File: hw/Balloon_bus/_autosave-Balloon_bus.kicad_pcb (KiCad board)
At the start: 16 copper layers, 96 x 89.9 mm, 14 parts, among them J1 3V3, J2 DEPLOY SENSOR, J3 SERVO, J4 SOLENOID, J5 LINEAR ACTUATOR, U1 XA1110, U2 MPU-9250-BREAKOUT-R, U3 BMP180-V2, U4 SN754410

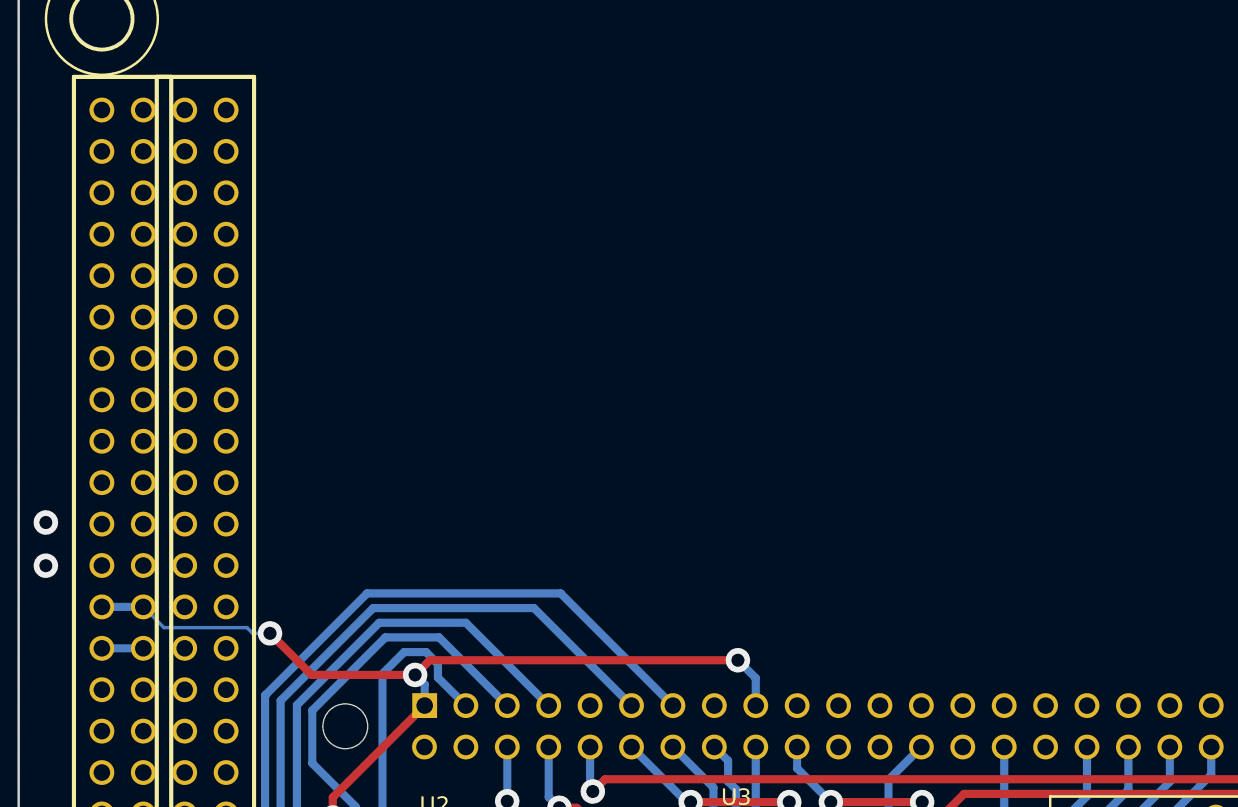
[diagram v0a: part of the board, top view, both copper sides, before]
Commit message: Zero unrouted tracks. Sensors and GPS schematics added to their respective libraries.
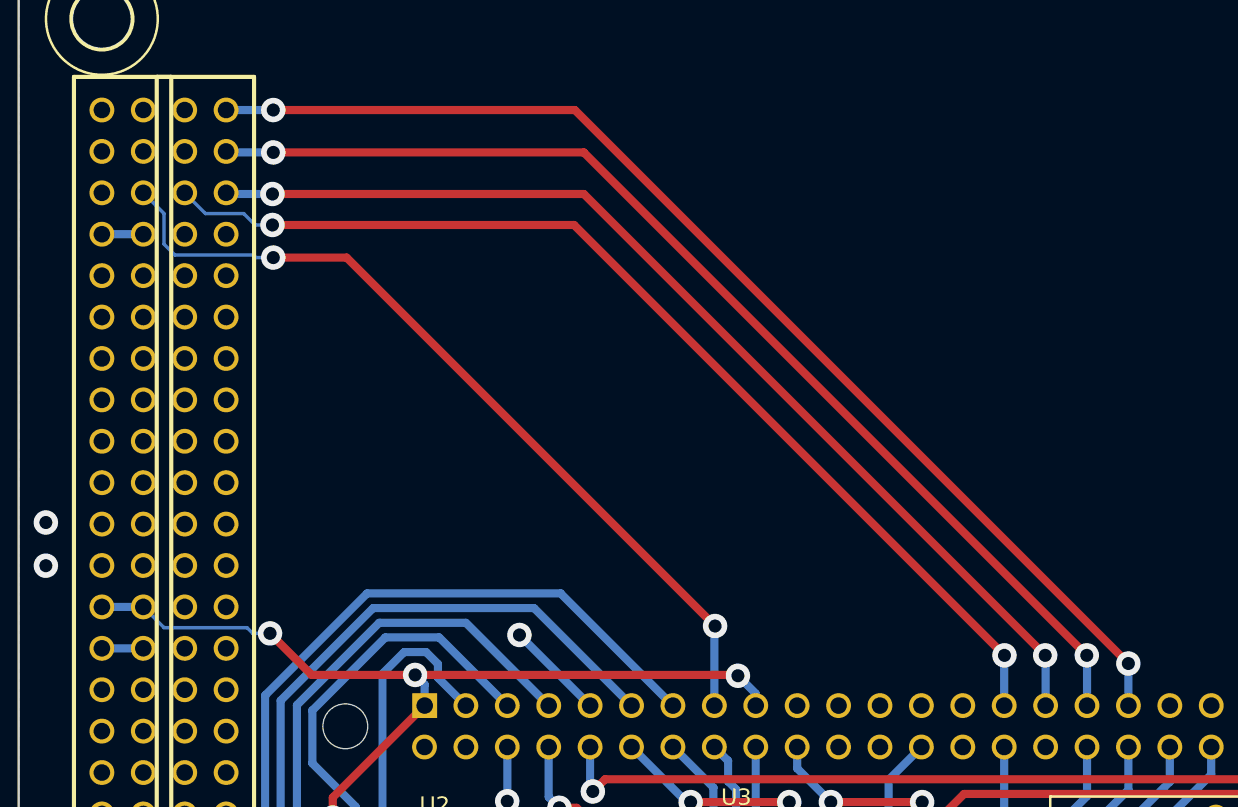
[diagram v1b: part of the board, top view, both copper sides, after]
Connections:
- H1H2 pad 102: /GPIO22 -> Net-(H1H2-Pad102)
- H1H2 pad 47: /GPIO4 -> /GPIO6
- H1H2 pad 49: /GPIO6 -> /GPIO13
- H1H2 pad 50: /GPIO12 -> Net-(H1H2-Pad50)
- H1H2 pad 51: /GPIO13 -> /GPIO19
- H1H2 pad 99: /GPIO19 -> /GPIO22
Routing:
- net /GPIO19: track 0.00 -> 72.0 mm, vias 0 -> 2
- net /GPIO13: track 0.00 -> 68.7 mm, vias 0 -> 2
- net /GPIO5: track 0.00 -> 65.1 mm, vias 0 -> 2
- net /GPIO6: track 0.00 -> 65.1 mm, vias 0 -> 2
- net /GPIO22: track 0.00 -> 52.1 mm, vias 0 -> 2
- net /GND: track 53.4 -> 59.5 mm, vias 19 -> 20
- net /VBATT: track 0.00 -> 2.54 mm
- net /3V3: track 221.7 -> 220.4 mm
